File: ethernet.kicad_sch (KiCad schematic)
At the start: 91 parts, among them IC2 ACPL-217-500E, J2 5-2337992-8, U13 TPS2373-4RGWR, U6 KSZ9031RNXCA, Y1 ABM8G-25.000MHZ-18-D2Y-T

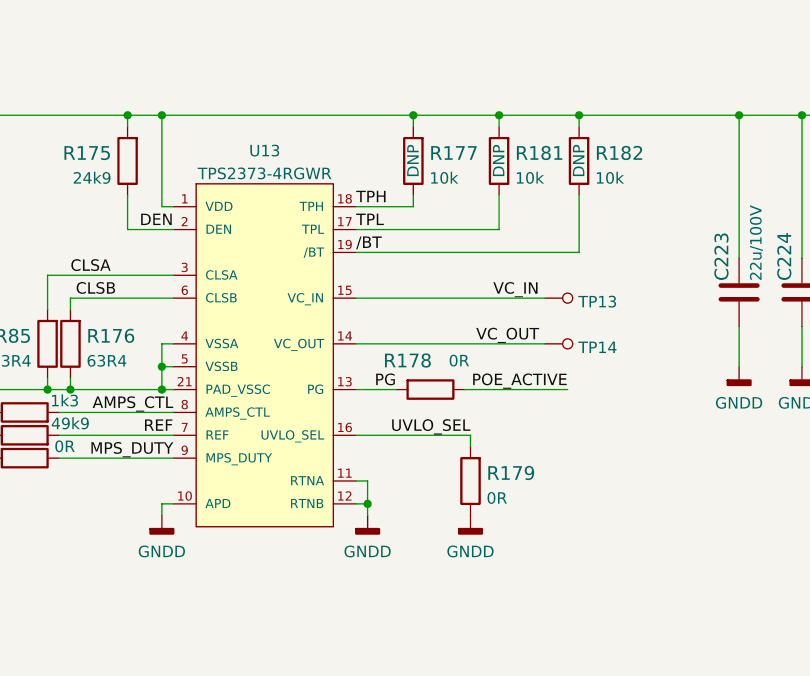
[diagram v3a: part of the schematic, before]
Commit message: Replace PoE IC to TPS2372-3RGWR with improved footprint
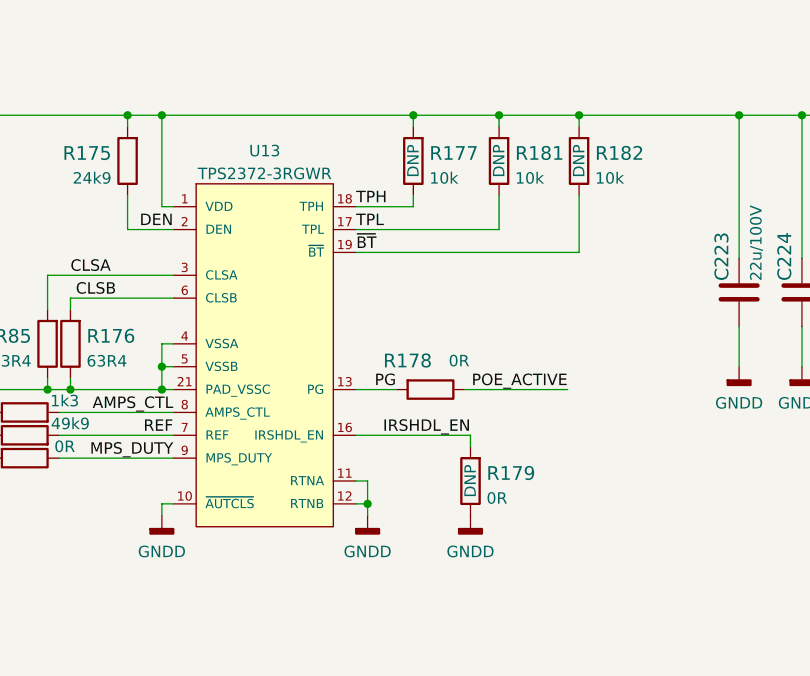
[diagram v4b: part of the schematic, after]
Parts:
- removed TP13, TP14: TP_SMD1MM, data-center-dram-tester-footprints:Testpoint_smd_1mm, symbol data-center-dram-tester:TP_SMD1MM
- removed U13: TPS2373-4RGWR, data-center-dram-tester-footprints:QFN65P500X500X100-21N, symbol data-center-dram-tester:TPS2373-4RGWR
- added U13: TPS2372-3RGWR, antmicro-footprints:Texas_RGW0020B, symbol antmicroPMICPowerDistributionSwitchesLoadDrivers:TPS2372-3RGWR
- R179: DNP (none) -> DNP
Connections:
- net AMPS_CTL: now also U13.8 (AMPS_CTL)
- net CLSA: now also U13.3 (CLSA)
- net CLSB: now also U13.6 (CLSB)
- net DEN: now also U13.2 (DEN)
- net GNDD: now also U13.10 (~{AUTCLS}), U13.11 (RTNA), U13.12 (RTNB)
- net MPS_DUTY: now also U13.9 (MPS_DUTY)
- net PG: now also U13.13 (PG)
- net REF: now also U13.7 (REF)
- net TPH: now also U13.18 (TPH)
- net TPL: now also U13.17 (TPL)
- net VDD: now also U13.1 (VDD)
- net VSS: now also U13.21 (PAD_VSSC), U13.4 (VSSA), U13.5 (VSSB)
- net UVLO_SEL renamed IRSHDL_EN
- net IRSHDL_EN: now also U13.16 (IRSHDL_EN)
- net /BT renamed ~{BT}
- net ~{BT}: now also U13.19 (~{BT})
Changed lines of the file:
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@@
     (stroke (width 0) (type default) (color 0 0 0 0))
   )
-  (wire (pts (xy 259.715 224.79) (xy 280.67 224.79))
-    (stroke (width 0) (type default) (color 0 0 0 0))
-  )
   (wire (pts (xy 336.55 118.11) (xy 328.295 118.11))
     (stroke (width 0) (type default) (color 0 0 0 0))
@@
     (stroke (width 0) (type default) (color 0 0 0 0))
   )
-  (wire (pts (xy 259.715 219.71) (xy 280.67 219.71))
-    (stroke (width 0) (type default) (color 0 0 0 0))
-  )
   (wire (pts (xy 336.55 130.81) (xy 328.295 130.81))
     (stroke (width 0) (type default) (color 0 0 0 0))
@@
     (effects (font (size 1.27 1.27)) (justify left bottom))
   )
-  (label "{slash}BT" (at 259.715 214.63 0)
+  (label "~{BT}" (at 259.715 214.63 0)
     (effects (font (size 1.27 1.27)) (justify left bottom))
   )
@@
     (effects (font (size 1.27 1.27)) (justify left bottom))
   )
-  (label "VC_OUT" (at 280.035 224.79 180)
-    (effects (font (size 1.27 1.27)) (justify right bottom))
-  )
   (label "PAIR_78" (at 34.925 233.045 0)
     (effects (font (size 1.27 1.27)) (justify left bottom))
@@
     (effects (font (size 1.27 1.27)) (justify right bottom))
   )
-  (label "VC_IN" (at 280.035 219.71 180)
-    (effects (font (size 1.27 1.27)) (justify right bottom))
-  )
   (label "PAIR_910" (at 34.925 235.585 0)
     (effects (font (size 1.27 1.27)) (justify left bottom))
@@
     (effects (font (size 1.27 1.27)) (justify right bottom))
   )
-  (label "UVLO_SEL" (at 272.415 234.95 180)
+  (label "IRSHDL_EN" (at 272.415 234.95 180)
     (effects (font (size 1.27 1.27)) (justify right bottom))
   )
@@
     (pin "2")
   )
-  (symbol (lib_id "data-center-dram-tester:TP_SMD1MM") (at 283.21 219.71 90) (mirror x) (unit 1)
+  (symbol (lib_id "data-center-dram-tester:GNDD") (at 342.265 217.17 0) (unit 1)
     (in_bom yes) (on_board yes) (fields_autoplaced)
-    (property "Reference" "TP13" (id 0) (at 284.4038 220.1438 90)
-      (effects (font (size 1.27 1.27)) (justify right))
-    )
-    (property "Value" "TP_SMD1MM" (id 1) (at 285.75 219.71 0)
+    (property "Reference" "#PWR0320" (id 0) (at 342.265 223.52 0)
       (effects (font (size 1.27 1.27)) hide)
     )
-    (property "Footprint" "data-center-dram-tester-footprints:Testpoint_smd_1mm" (id 2) (at 278.13 224.79 0)
-      (effects (font (size 1.524 1.524)) (justify left) hide)
+    (property "Value" "GNDD" (id 1) (at 342.265 221.2324 0))
+    (property "Footprint" "" (id 2) (at 342.265 217.17 0)
+      (effects (font (size 1.27 1.27)) hide)
     )
-    (property "Datasheet" "" (id 3) (at 275.59 224.79 0)
-      (effects (font (size 1.524 1.524)) (justify left) hide)
+    (property "Datasheet" "" (id 3) (at 342.265 217.17 0)
+      (effects (font (size 1.27 1.27)) hide)
     )
     (pin "1")
   )
-  (symbol (lib_id "data-center-dram-tester:GNDD") (at 342.265 217.17 0) (unit 1)
+  (symbol (lib_id "antmicroPMICPowerDistributionSwitchesLoadDrivers:TPS2372-3RGWR") (at 249.555 232.41 0) (unit 1)
     (in_bom yes) (on_board yes) (fields_autoplaced)
-    (property "Reference" "#PWR0320" (id 0) (at 342.265 223.52 0)
-      (effects (font (size 1.27 1.27)) hide)
+    (property "Reference" "U13" (id 0) (at 249.555 203.361 0))
+    (property "Value" "TPS2372-3RGWR" (id 1) (at 249.555 205.8979 0))
+    (property "Footprint" "antmicro-footprints:Texas_RGW0020B" (id 2) (at 243.205 252.73 0)
+      (effects (font (size 1.27 1.27)) (justify left bottom) hide)
     )
-    (property "Value" "GNDD" (id 1) (at 342.265 221.2324 0))
-    (property "Footprint" "" (id 2) (at 342.265 217.17 0)
+    (property "Datasheet" "" (id 3) (at 249.555 232.41 0)
+      (effects (font (size 1.27 1.27)) (justify left bottom) hide)
+    )
+    (property "MPN" "TPS2372-3RGWR" (id 4) (at 250.825 248.92 0)
       (effects (font (size 1.27 1.27)) hide)
     )
-    (property "Datasheet" "" (id 3) (at 342.265 217.17 0)
+    (property "Manufacturer" "Texas Instruments" (id 5) (at 250.825 246.38 0)
       (effects (font (size 1.27 1.27)) hide)
     )
     (pin "1")
+    (pin "10")
+    (pin "11")
+    (pin "12")
+    (pin "13")
+    (pin "14")
+    (pin "15")
+    (pin "16")
+    (pin "17")
+    (pin "18")
+    (pin "19")
+    (pin "2")
+    (pin "21")
+    (pin "3")
+    (pin "4")
+    (pin "5")
+    (pin "6")
+    (pin "7")
+    (pin "8")
+    (pin "9")
   )
   (symbol (lib_id "data-center-dram-tester:R_32k4_0402") (at 325.755 213.995 90) (unit 1)
@@
     (pin "2")
   )
-  (symbol (lib_id "data-center-dram-tester:TPS2373-4RGWR") (at 249.555 232.41 0) (unit 1)
-    (in_bom yes) (on_board yes) (fields_autoplaced)
-    (property "Reference" "U13" (id 0) (at 249.555 203.361 0))
-    (property "Value" "TPS2373-4RGWR" (id 1) (at 249.555 205.8979 0))
-    (property "Footprint" "data-center-dram-tester-footprints:QFN65P500X500X100-21N" (id 2) (at 229.235 250.19 0)
-      (effects (font (size 1.27 1.27)) (justify left bottom) hide)
-    )
-    (property "Datasheet" "" (id 3) (at 249.555 232.41 0)
-      (effects (font (size 1.27 1.27)) (justify left bottom) hide)
-    )
-    (property "MPN" "TPS2373-4RGWR" (id 4) (at 249.555 252.73 0)
-      (effects (font (size 1.27 1.27)) hide)
-    )
-    (property "Manufacturer" "Texas Instruments" (id 5) (at 249.555 255.27 0)
-      (effects (font (size 1.27 1.27)) hide)
-    )
-    (pin "1")
-    (pin "10")
-    (pin "11")
-    (pin "12")
-    (pin "13")
-    (pin "14")
-    (pin "15")
-    (pin "16")
-    (pin "17")
-    (pin "18")
-    (pin "19")
-    (pin "2")
-    (pin "21")
-    (pin "3")
-    (pin "4")
-    (pin "5")
-    (pin "6")
-    (pin "7")
-    (pin "8")
-    (pin "9")
-  )
   (symbol (lib_id "data-center-dram-tester:R_0R_0603") (at 267.97 229.87 180) (unit 1)
     (in_bom yes) (on_board yes)
@@
   )
   (symbol (lib_id "data-center-dram-tester:R_0R_0603") (at 272.415 240.03 90) (unit 1)
-    (in_bom yes) (on_board yes) (fields_autoplaced)
+    (in_bom yes) (on_board yes)
     (property "Reference" "R179" (id 0) (at 274.193 239.1954 90)
       (effects (font (size 1.524 1.524)) (justify right))
@@
       (effects (font (size 1.27 1.27)) (justify right))
     )
+    (property "DNP" "DNP" (id 7) (at 272.415 240.03 0))
     (pin "1")
     (pin "2")
@@
     (pin "2")
   )
-  (symbol (lib_id "data-center-dram-tester:TP_SMD1MM") (at 283.21 224.79 90) (mirror x) (unit 1)
-    (in_bom yes) (on_board yes) (fields_autoplaced)
-    (property "Reference" "TP14" (id 0) (at 284.4038 225.2238 90)
-      (effects (font (size 1.27 1.27)) (justify right))
-    )
-    (property "Value" "TP_SMD1MM" (id 1) (at 285.75 224.79 0)
-      (effects (font (size 1.27 1.27)) hide)
-    )
-    (property "Footprint" "data-center-dram-tester-footprints:Testpoint_smd_1mm" (id 2) (at 278.13 229.87 0)
-      (effects (font (size 1.524 1.524)) (justify left) hide)
-    )
-    (property "Datasheet" "" (id 3) (at 275.59 229.87 0)
-      (effects (font (size 1.524 1.524)) (justify left) hide)
-    )
-    (pin "1")
-  )
   (symbol (lib_id "data-center-dram-tester:C_22u_2220_100V") (at 309.245 219.075 0) (unit 1)

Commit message: B2B FMC HPC connector added, recconected PCIe to new connector, added ETH mux
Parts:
- added C?: C_10n_0402, data-center-dram-tester-footprints:0402-cap, symbol data-center-dram-tester:C_10n_0402
- added C?: C_4u7_0402, data-center-dram-tester-footprints:0402-cap, symbol data-center-dram-tester:C_4u7_0402
- added U?: TS3L500, antmicro-footprints:Texas_RHU0056A, symbol antmicroLogicSignalSwitchesMultiplexersDecoders:TS3L500
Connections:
- net ETH1_N: now also U?.3 (A1); no longer J2.2 (P2)
- net ETH1_P: now also U?.2 (A0); no longer J2.1 (P1)
- net ETH2_N: now also U?.8 (A3); no longer J2.6 (P6)
- net ETH2_P: now also U?.7 (A2); no longer J2.3 (P3)
- net ETH3_N: now also U?.12 (A5); no longer J2.8 (P8)
- net ETH3_P: now also U?.11 (A4); no longer J2.7 (P7)
- net ETH4_N: now also U?.15 (A7); no longer J2.10 (P10)
- net ETH4_P: now also U?.14 (A6); no longer J2.9 (P9)
- net GND: now also C?.2, C?.2, U?.1 (GND), U?.13 (GND), U?.16 (GND), U?.19 (LED0), U?.21 (GND), U?.24 (GND), U?.28 (GND), U?.33 (GND), U?.39 (GND), U?.44 (GND), U?.49 (GND), U?.53 (GND), U?.55 (GND), U?.57 (EPAD), U?.6 (GND), U?.9 (GND)
- net LED_LINK: now also U?.20 (LED1); no longer J2.18
- net LED_SPD: now also U?.54 (LED2); no longer J2.16
- net 3V3_SYS renamed VCC
- net VCC: now also C?.1, C?.1, U?.10 (VCC), U?.18 (VCC), U?.27 (VCC), U?.38 (VCC), U?.4 (VCC), U?.50 (VCC), U?.56 (VCC)
- new net EXT_ETH1_N: U?.45 (1B2)
- new net EXT_ETH1_P: U?.46 (0B2)
- new net EXT_ETH2_N: U?.40 (3B2)
- new net EXT_ETH2_P: U?.41 (2B2)
- new net EXT_ETH3_N: U?.34 (5B2)
- new net EXT_ETH3_P: U?.35 (4B2)
- new net EXT_ETH4_N: U?.29 (7B2)
- new net EXT_ETH4_P: U?.30 (6B2)
- new net EXT_LED_LINK: U?.26 (1LED2), U?.51 (2LED2)
- new net INT_ETH1_N: J2.2 (P2), U?.47 (1B1)
- new net INT_ETH1_P: J2.1 (P1), U?.48 (0B1)
- new net INT_ETH2_N: J2.6 (P6), U?.42 (3B1)
- new net INT_ETH2_P: J2.3 (P3), U?.43 (2B1)
- new net INT_ETH3_N: J2.8 (P8), U?.36 (5B1)
- new net INT_ETH3_P: J2.7 (P7), U?.37 (4B1)
- new net INT_ETH4_N: J2.10 (P10), U?.31 (7B1)
- new net INT_ETH4_P: J2.9 (P9), U?.32 (6B1)
- new net INT_LED_LINK: J2.18, U?.23 (1LED1)
- new net INT_LED_SPD: J2.16, U?.52 (2LED1)
- no-connect marks 2 -> 4
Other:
- moved on the sheet: C147, C148, R68, R69, R70, R71, R72, R73, R74, R75, R76, R77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

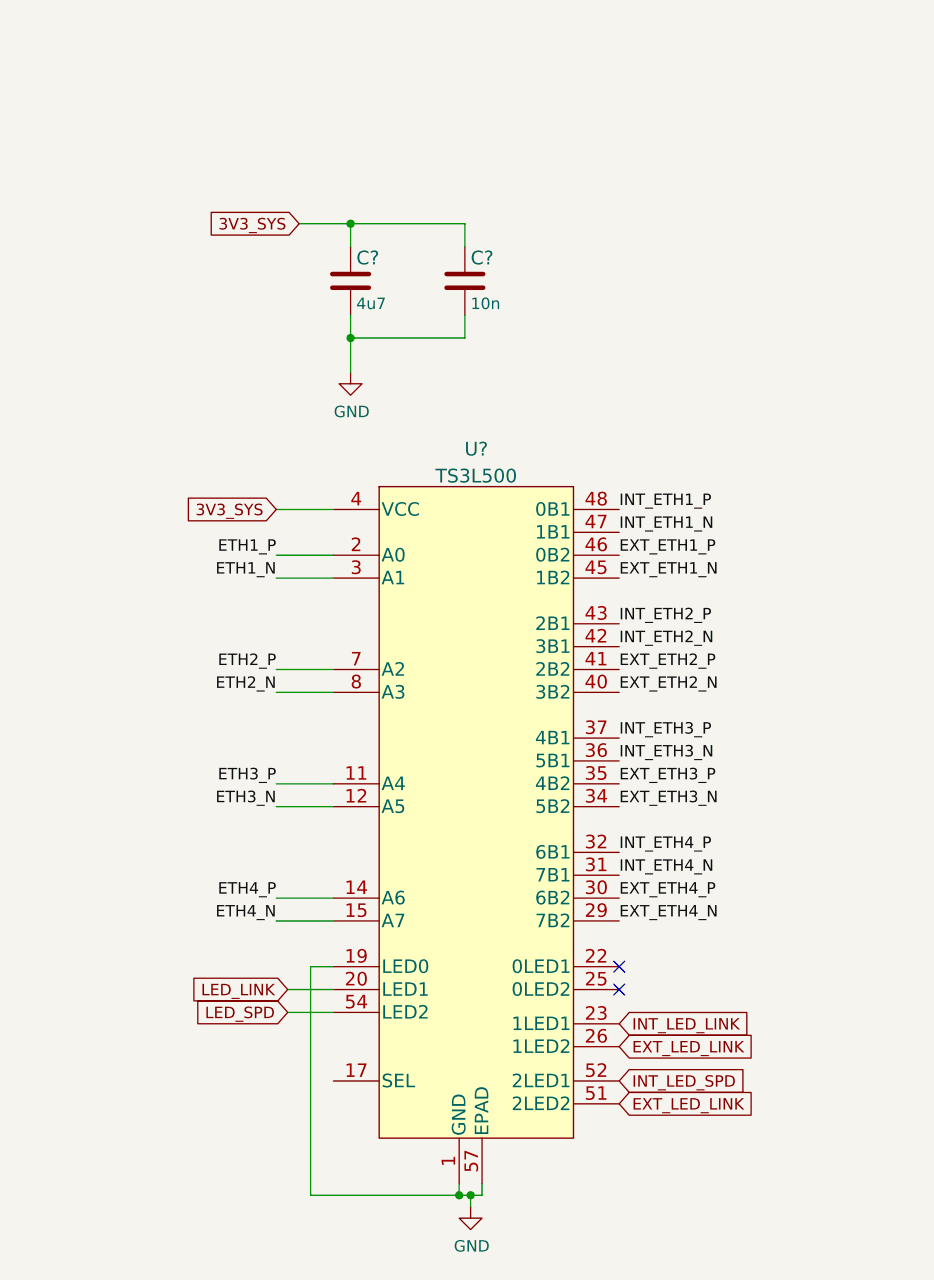
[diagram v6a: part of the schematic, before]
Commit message: Connect ETH mux, connect AUX_JTAG to FMC connector, add RC filter for HOT_SWAP_BUTTON signal
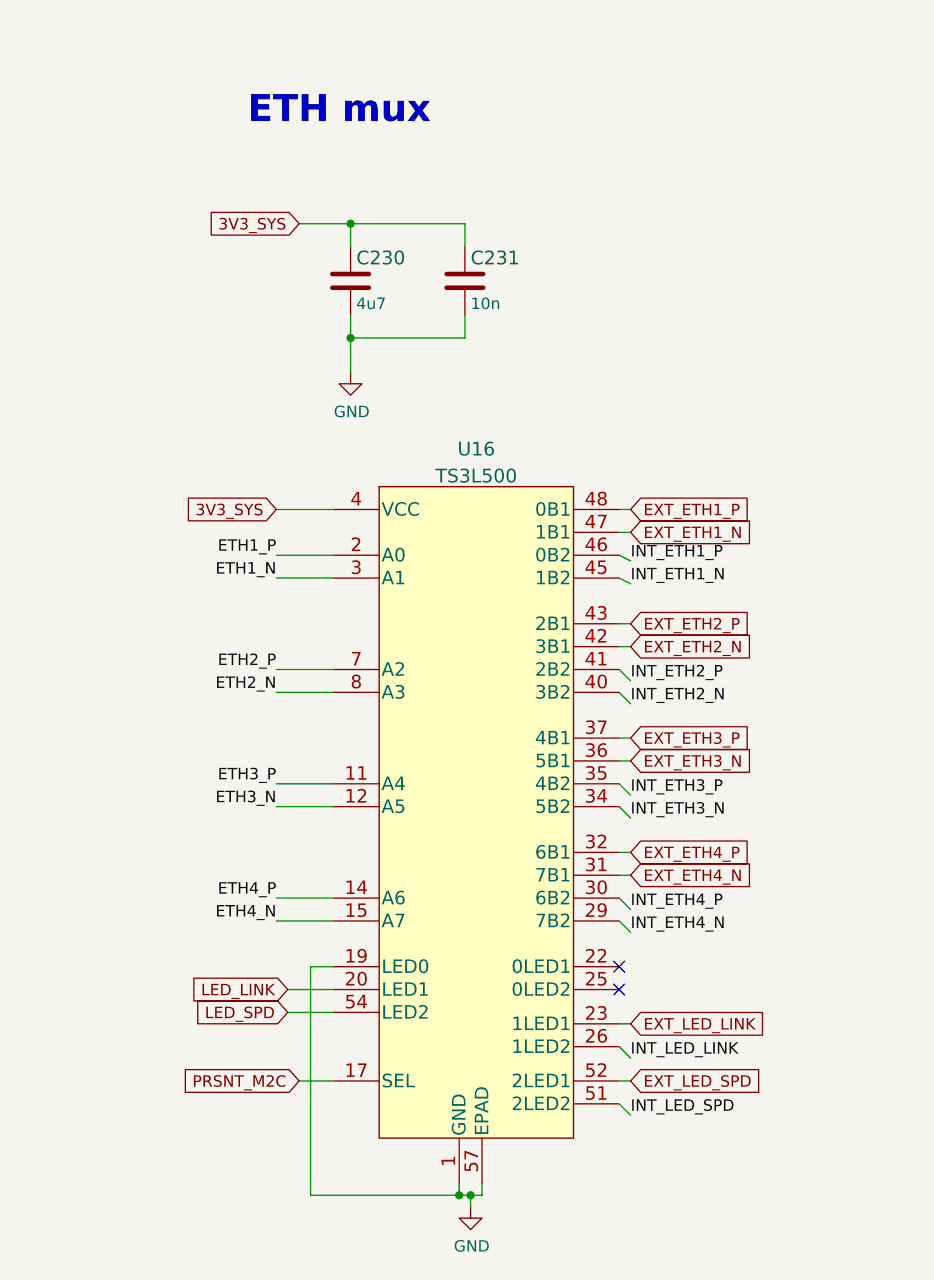
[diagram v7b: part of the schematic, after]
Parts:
- gave numbers to parts that had none: 3
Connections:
- net EXT_ETH1_N: now also U16.47 (1B1); no longer U16.45 (1B2)
- net EXT_ETH1_P: now also U16.48 (0B1); no longer U16.46 (0B2)
- net EXT_ETH2_N: now also U16.42 (3B1); no longer U16.40 (3B2)
- net EXT_ETH2_P: now also U16.43 (2B1); no longer U16.41 (2B2)
- net EXT_ETH3_N: now also U16.36 (5B1); no longer U16.34 (5B2)
- net EXT_ETH3_P: now also U16.37 (4B1); no longer U16.35 (4B2)
- net EXT_ETH4_N: now also U16.31 (7B1); no longer U16.29 (7B2)
- net EXT_ETH4_P: now also U16.32 (6B1); no longer U16.30 (6B2)
- net EXT_LED_LINK: now also U16.23 (1LED1); no longer U16.26 (1LED2), U16.51 (2LED2)
- net INT_ETH1_N: now also U16.45 (1B2); no longer U16.47 (1B1)
- net INT_ETH1_P: now also U16.46 (0B2); no longer U16.48 (0B1)
- net INT_ETH2_N: now also U16.40 (3B2); no longer U16.42 (3B1)
- net INT_ETH2_P: now also U16.41 (2B2); no longer U16.43 (2B1)
- net INT_ETH3_N: now also U16.34 (5B2); no longer U16.36 (5B1)
- net INT_ETH3_P: now also U16.35 (4B2); no longer U16.37 (4B1)
- net INT_ETH4_N: now also U16.29 (7B2); no longer U16.31 (7B1)
- net INT_ETH4_P: now also U16.30 (6B2); no longer U16.32 (6B1)
- net INT_LED_LINK: now also U16.26 (1LED2); no longer U16.23 (1LED1)
- net INT_LED_SPD: now also U16.51 (2LED2); no longer U16.52 (2LED1)
- net PRSNT_M2C: now reaches U16.17 (SEL)
- new net EXT_LED_SPD: U16.52 (2LED1)
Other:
- note added: "ETH mux"
